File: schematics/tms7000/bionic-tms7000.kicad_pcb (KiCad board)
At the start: 2 copper layers, 27.9 x 68.6 mm, 8 parts, among them J1 Bionic-P135, J2 Bionic-P245, U1 TMS70C02, U2 11AA010-I/TT

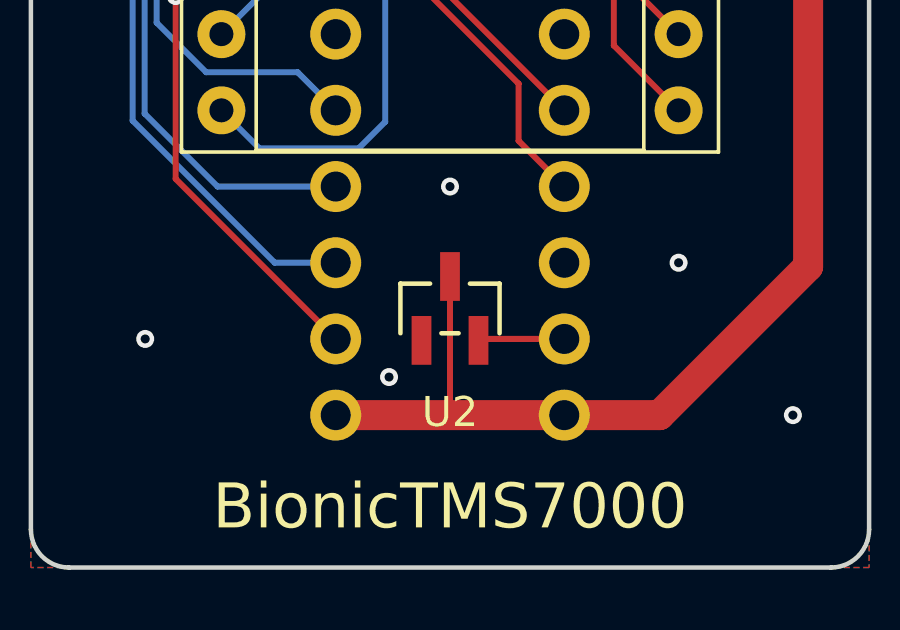
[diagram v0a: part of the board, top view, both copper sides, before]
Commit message: [TMS7000] Fix EEPROM pinout
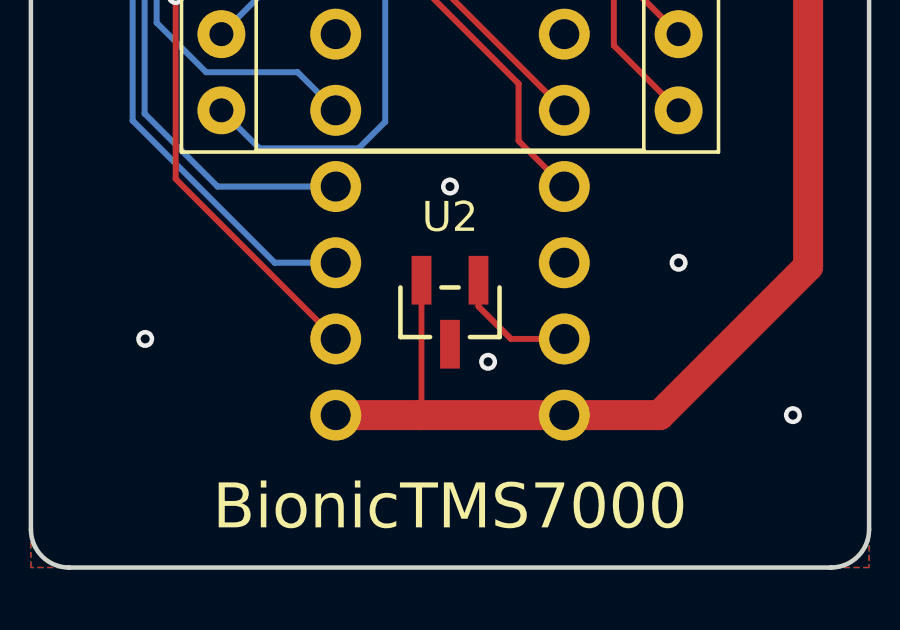
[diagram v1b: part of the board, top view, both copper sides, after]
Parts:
- U1: value TMS70C02 -> TMS7000
- moved U2 0.13 mm to (115.0, 130.1), turned to 180 degrees
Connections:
- U2 pad 1: GND -> Net-(J2-P57)
- U2 pad 2: Net-(J2-P57) -> VCC
- U2 pad 3: VCC -> GND
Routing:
- net VCC: track 104.6 -> 99.9 mm
- net Net-(J2-P57): track 5.69 -> 4.18 mm
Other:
- board text added: "Rev. 3"
- board text removed: "Rev. 2"

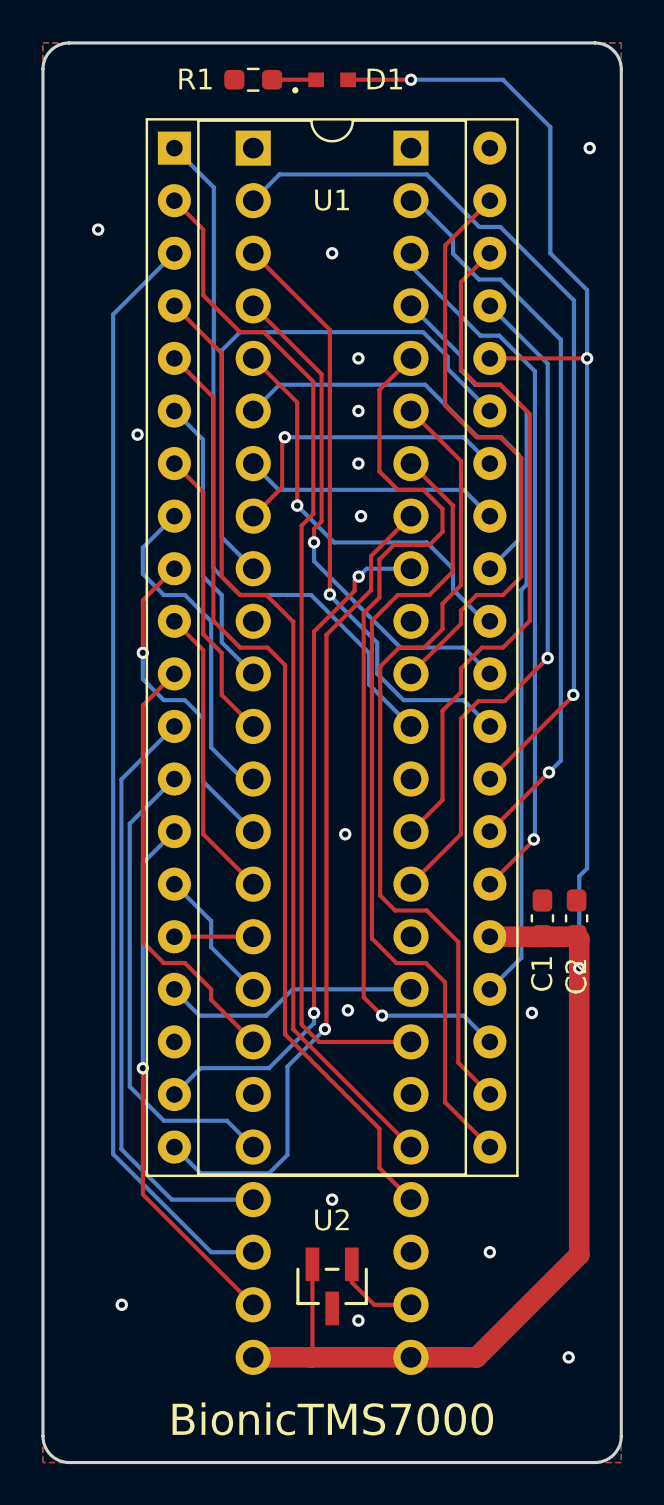
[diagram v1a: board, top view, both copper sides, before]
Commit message: [TMS7000] Shrink board size
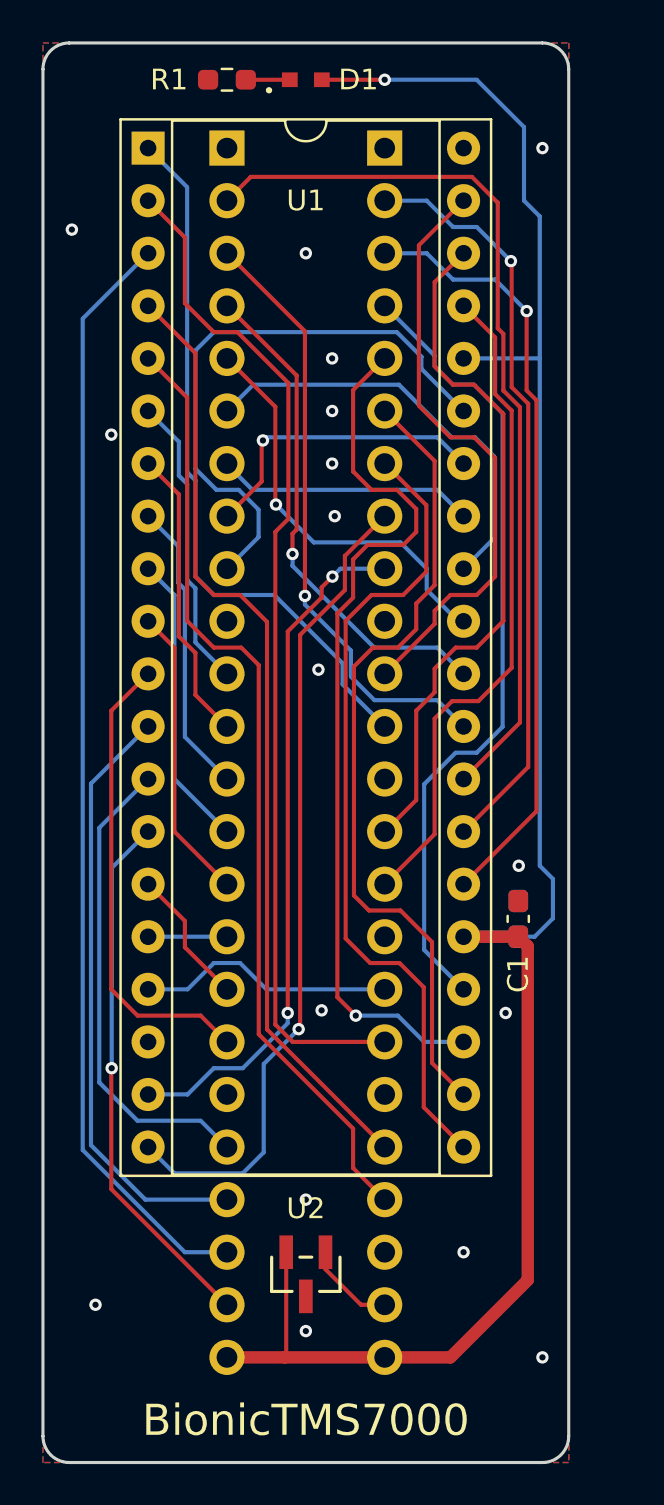
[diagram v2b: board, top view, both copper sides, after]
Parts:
- C2: moved to B.Cu
- moved C2 2.82 mm to (124.0, 112.3)
- moved U2 1.40 mm to (113.7, 129.5)
- moved D1 1.27 mm to (113.7, 71.8)
- moved J1 1.27 mm to (109.9, 75.1)
- moved J2 1.27 mm to (117.5, 75.1)
- moved R1 1.27 mm to (109.9, 71.8)
- moved U1 1.27 mm to (106.1, 75.1)
- moved C1 1.17 mm to (124.0, 112.3)
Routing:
- net /P21: track 34.4 -> 37.4 mm
- net /P32: track 16.4 -> 14.3 mm
- net /P22: track 36.8 -> 38.9 mm
- net /P17: track 26.4 -> 28.3 mm
- net /P33: track 16.1 -> 14.3 mm, vias 1 -> 0
- net /P37: track 21.2 -> 22.6 mm
- net VCC: track 99.9 -> 98.7 mm, vias 3 -> 1
- net /P20: track 35.7 -> 36.5 mm
- net /P44: track 32.6 -> 32.2 mm, vias 1 -> 0
- net /P10: track 43.3 -> 43.5 mm, vias 1 -> 0
- net GND: vias 16 -> 17
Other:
- board size 27.9 x 68.6 mm -> 25.4 x 68.6 mm

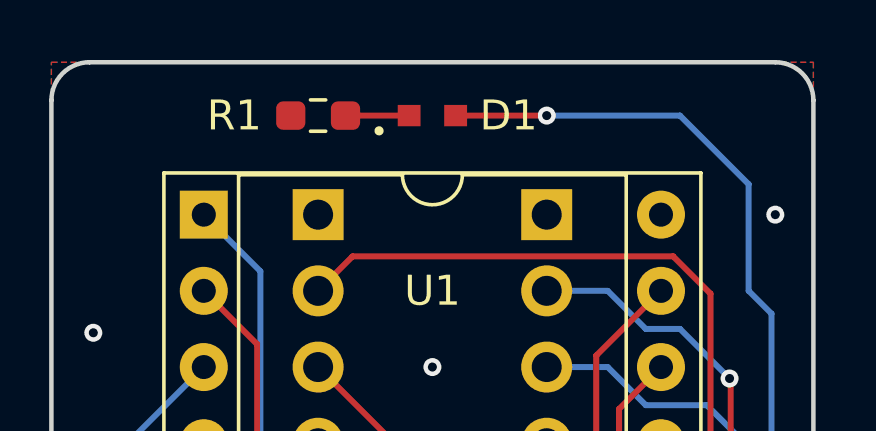
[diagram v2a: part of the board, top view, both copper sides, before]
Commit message: [schematics] Update LED footprint
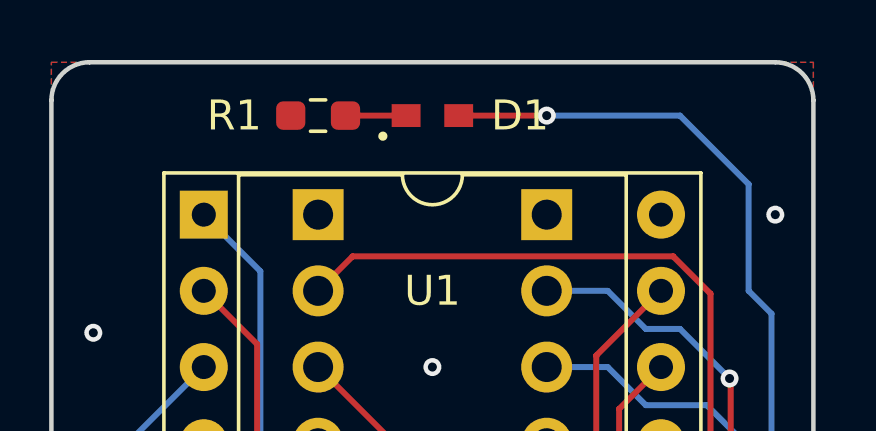
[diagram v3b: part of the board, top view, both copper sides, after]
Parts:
- D1: footprint 0-LocalLibrary:LED_CSL1901UW1_ROM -> 0-LocalLibrary:LED_CSL1901UW1_ROM-M

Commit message: [TMS7000] Cleanup schematics
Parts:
- D1: footprint 0-LocalLibrary:LED_CSL1901UW1_ROM-M -> rhom:LED_CSL1901UW1_ROM-M
- J1: footprint 0-LocalLibrary:Bionic-P135_Vertical -> bionic:Bionic-P135_Vertical
- J2: footprint 0-LocalLibrary:Bionic-P245_Vertical -> bionic:Bionic-P245_Vertical
- U1: value TMS7000 -> TMS7002; footprint 0-LocalLibrary:DIP-40_W15.24mm_Socket -> bionic:DIP-40_W15.24mm_Socket
- U2: footprint 0-LocalLibrary:SOT-23_MC_MCH-M -> microchip:SOT-23_MC_MCH-M
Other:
- rule pad_to_mask_clearance: 0.051 -> 0

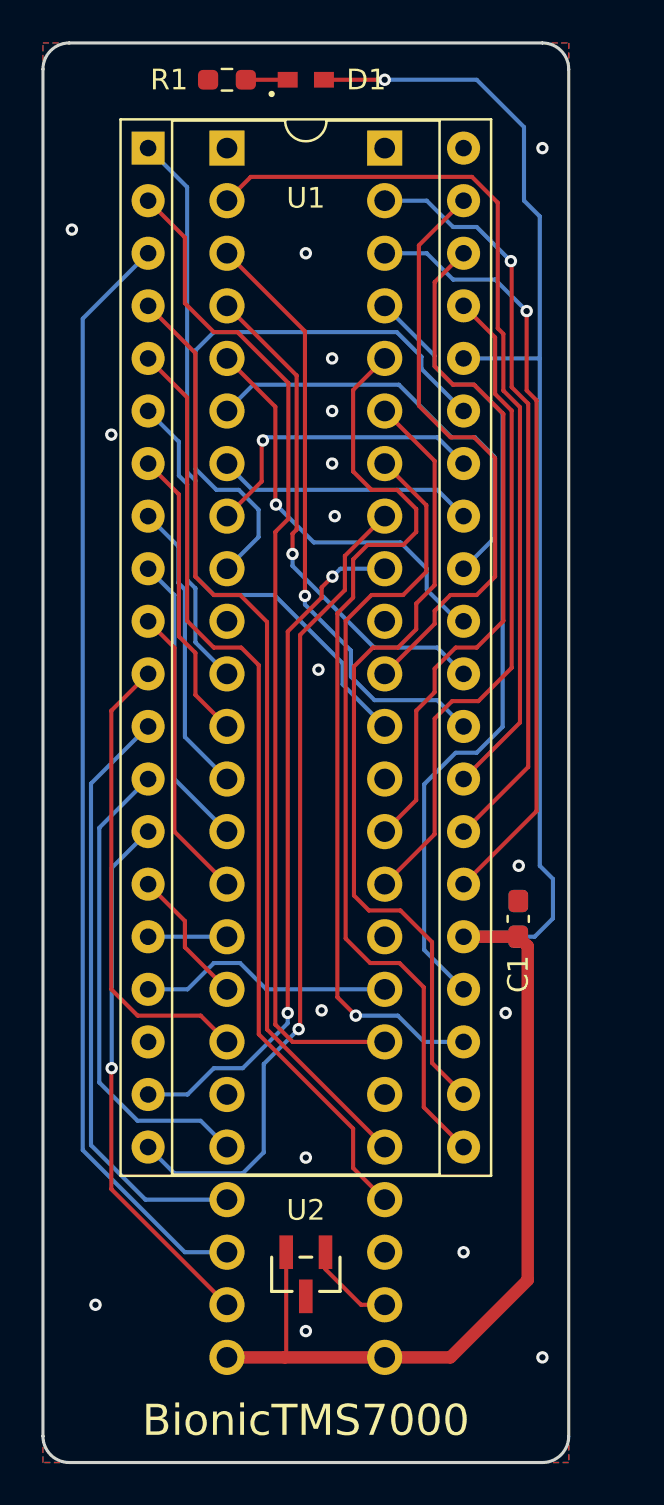
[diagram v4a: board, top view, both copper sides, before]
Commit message: [TMS7000] Update schematics
Remove unused pins from bionic connector
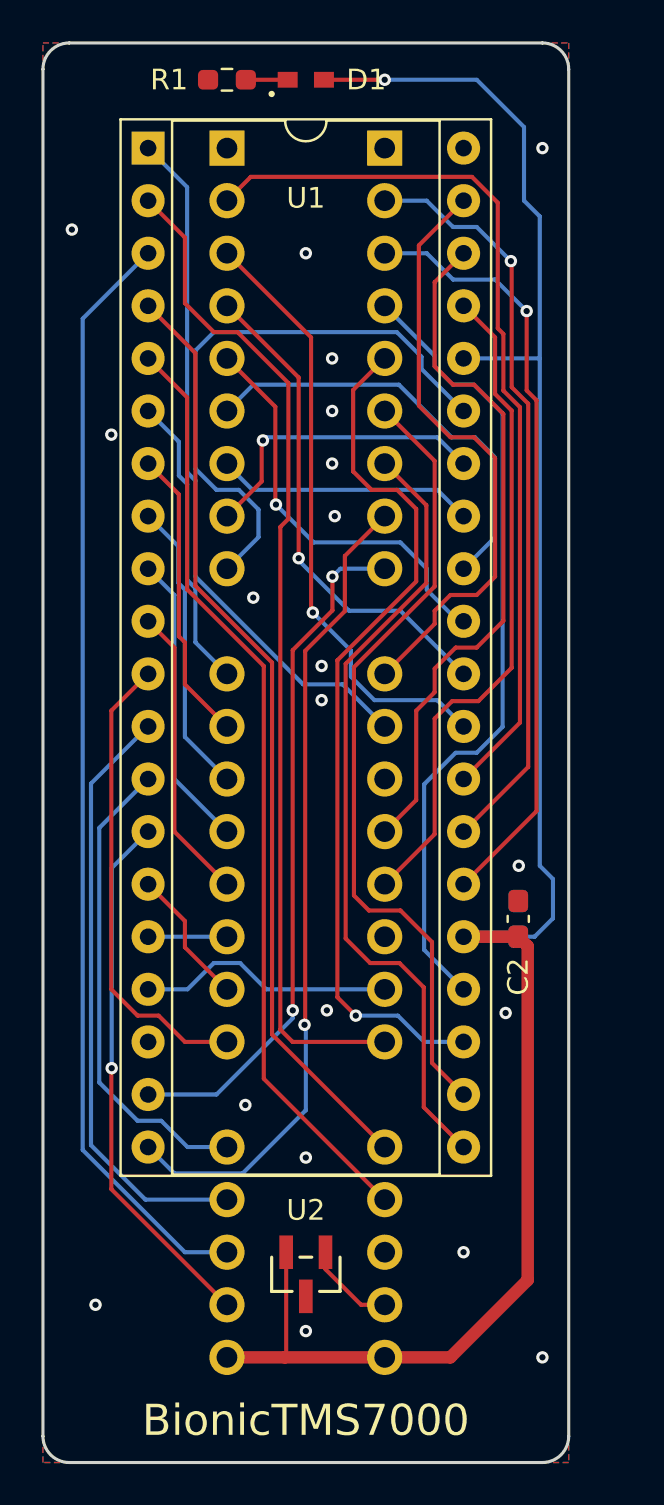
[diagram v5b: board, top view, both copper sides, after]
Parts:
- C1: moved to B.Cu
- C2: moved to F.Cu
- J1: footprint bionic:Bionic-P135_Vertical -> bionic:Bionic-P135_THT
- J2: footprint bionic:Bionic-P245_Vertical -> bionic:Bionic-P245_THT
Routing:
- net /P23: track 43.1 -> 42.0 mm
- net /P25: track 39.6 -> 38.7 mm
- net /P55: track 46.2 -> 45.4 mm
- net /P54: track 46.1 -> 45.4 mm
- net /P24: track 39.4 -> 38.7 mm
- net /P41: track 34.4 -> 33.8 mm
- net GND: vias 17 -> 20
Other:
- board text added: "Rev. 4"
- board text removed: "Rev. 3"
